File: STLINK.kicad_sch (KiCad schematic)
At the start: 1 part, among them J3 Conn_01x04_Pin

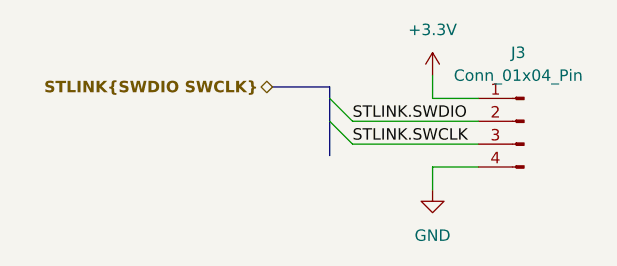
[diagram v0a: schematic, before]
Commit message: MOD : KiCad 8.0.1 -> 9.0.0. ADD : Codec power circuitry.
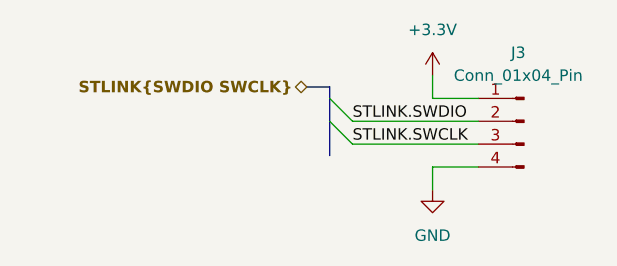
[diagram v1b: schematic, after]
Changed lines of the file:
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@@
 (kicad_sch
-	(version 20231120)
+	(version 20250114)
 	(generator "eeschema")
-	(generator_version "8.0")
+	(generator_version "9.0")
 	(paper "A4")
 	(bus_entry
@@
 	(bus
 		(pts
-			(xy 138.43 92.71) (xy 144.78 92.71)
+			(xy 142.24 92.71) (xy 144.78 92.71)
 		)
 		(stroke
@@
 	(hierarchical_label "STLINK{SWDIO SWCLK}"
 		(shape bidirectional)
-		(at 138.43 92.71 180)
-		(fields_autoplaced yes)
+		(at 142.24 92.71 180)
 		(effects
 			(font

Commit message: ADD : Footprint assignment. FIX : Various ERC rules.
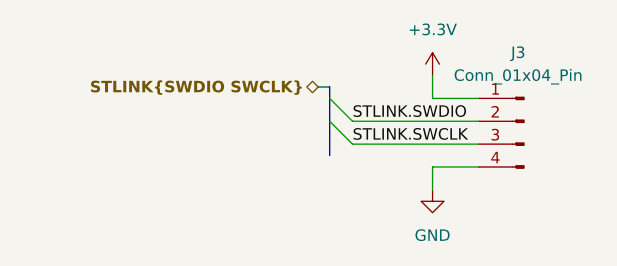
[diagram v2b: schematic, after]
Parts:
- J3: footprint (none) -> Connector_PinHeader_2.54mm:PinHeader_1x04_P2.54mm_Vertical
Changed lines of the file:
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@@
 	(bus
 		(pts
-			(xy 142.24 92.71) (xy 144.78 92.71)
+			(xy 143.51 92.71) (xy 144.78 92.71)
 		)
 		(stroke
@@
 	(hierarchical_label "STLINK{SWDIO SWCLK}"
 		(shape bidirectional)
-		(at 142.24 92.71 180)
+		(at 143.51 92.71 180)
 		(effects
 			(font
@@
 			)
 		)
-		(property "Footprint" ""
+		(property "Footprint" "Connector_PinHeader_2.54mm:PinHeader_1x04_P2.54mm_Vertical"
 			(at 166.37 96.52 0)
 			(effects
